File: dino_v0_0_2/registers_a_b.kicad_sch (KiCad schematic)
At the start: 11 parts, among them U31 74LS373, U32 74LS373, U33 74LS373, U35 74LS373, U41 74LS245, U42 74LS245, U43 74LS245, U44 74LS245, U5 74LS08, U57 74LS02, U66 74LS02

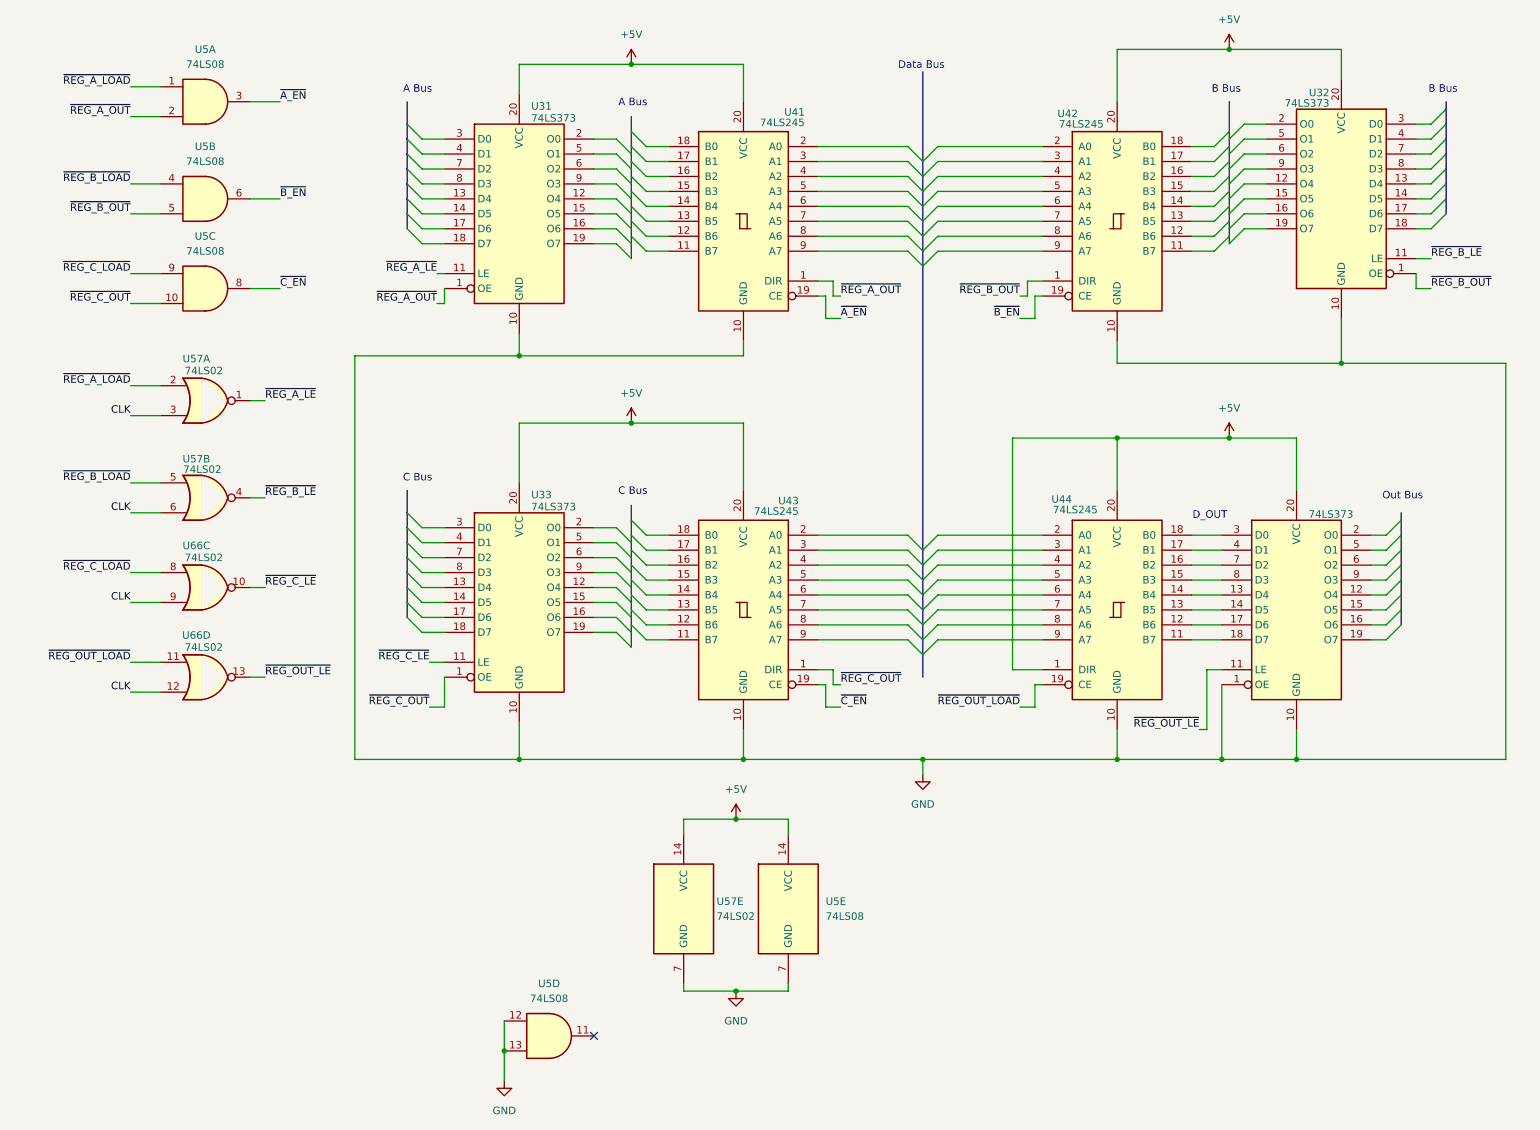
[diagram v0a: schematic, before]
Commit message: DINO v0.0.3: complete ALU/control-word, add MAR+reset sheets, wire reset circuit
ALU sheet: flags register moved from '173 (not in stock) to '273 + a '157
mux to emulate the missing load-enable pins; Z-detect built from a NOR+AND
De Morgan tree instead of a '260; ALU_CIN built from NAND(SA1,SA0) reusing
two already-placed spare gates instead of a dedicated XOR/'86. Sheet is
now fully wired and netlist-clean.

Control word sheet: all 16 CW bits assigned and wired (3x '138 decoders
for the load/source/misc fields, direct bus taps for HALT/PC_MAR_MUX/
PC_UP/END and the ALU SA[2:0] select). Found and fixed several cross-
sheet signal-name mismatches this uncovered (OUT_REG_LOAD/REG_OUT_LOAD,
PC_MAR_MUX/PC_MUX, T-state counter labels, a mirror-reversed IRB->ROM-
address buffer in microcode).

New: MAR and reset sheets, wired into the root hierarchy. Reset circuit
is a from-scratch design: RC+button+74HC14 Schmitt front end feeds the
async PRESET of the clock cluster's spare '74 half (U27B), synchronizing
release to CLK; its Q/~Q fan out to the flags register, the T-state
counter's clear, and (OR'd with the existing microcode-driven PC_CLEAR,
reusing spare gates on the same '02) the PC counters' clear.

Deprecated 7 schematic files no longer referenced by the root sheet's
hierarchy into dino_v0_0_2/deprecated/. Added docs/notes/kicad_netlist.py,
a .kicad_sch connectivity auditor (pin/net resolution incl. buses and
same-name local-label merging) used throughout this session to find the
above bugs; archived completed-work docs into docs/notes/Done/ and
rewrote dino_session_state.md as the current authoritative state+TODO.

Co-Authored-By: Claude Sonnet 5 <noreply@anthropic.com>
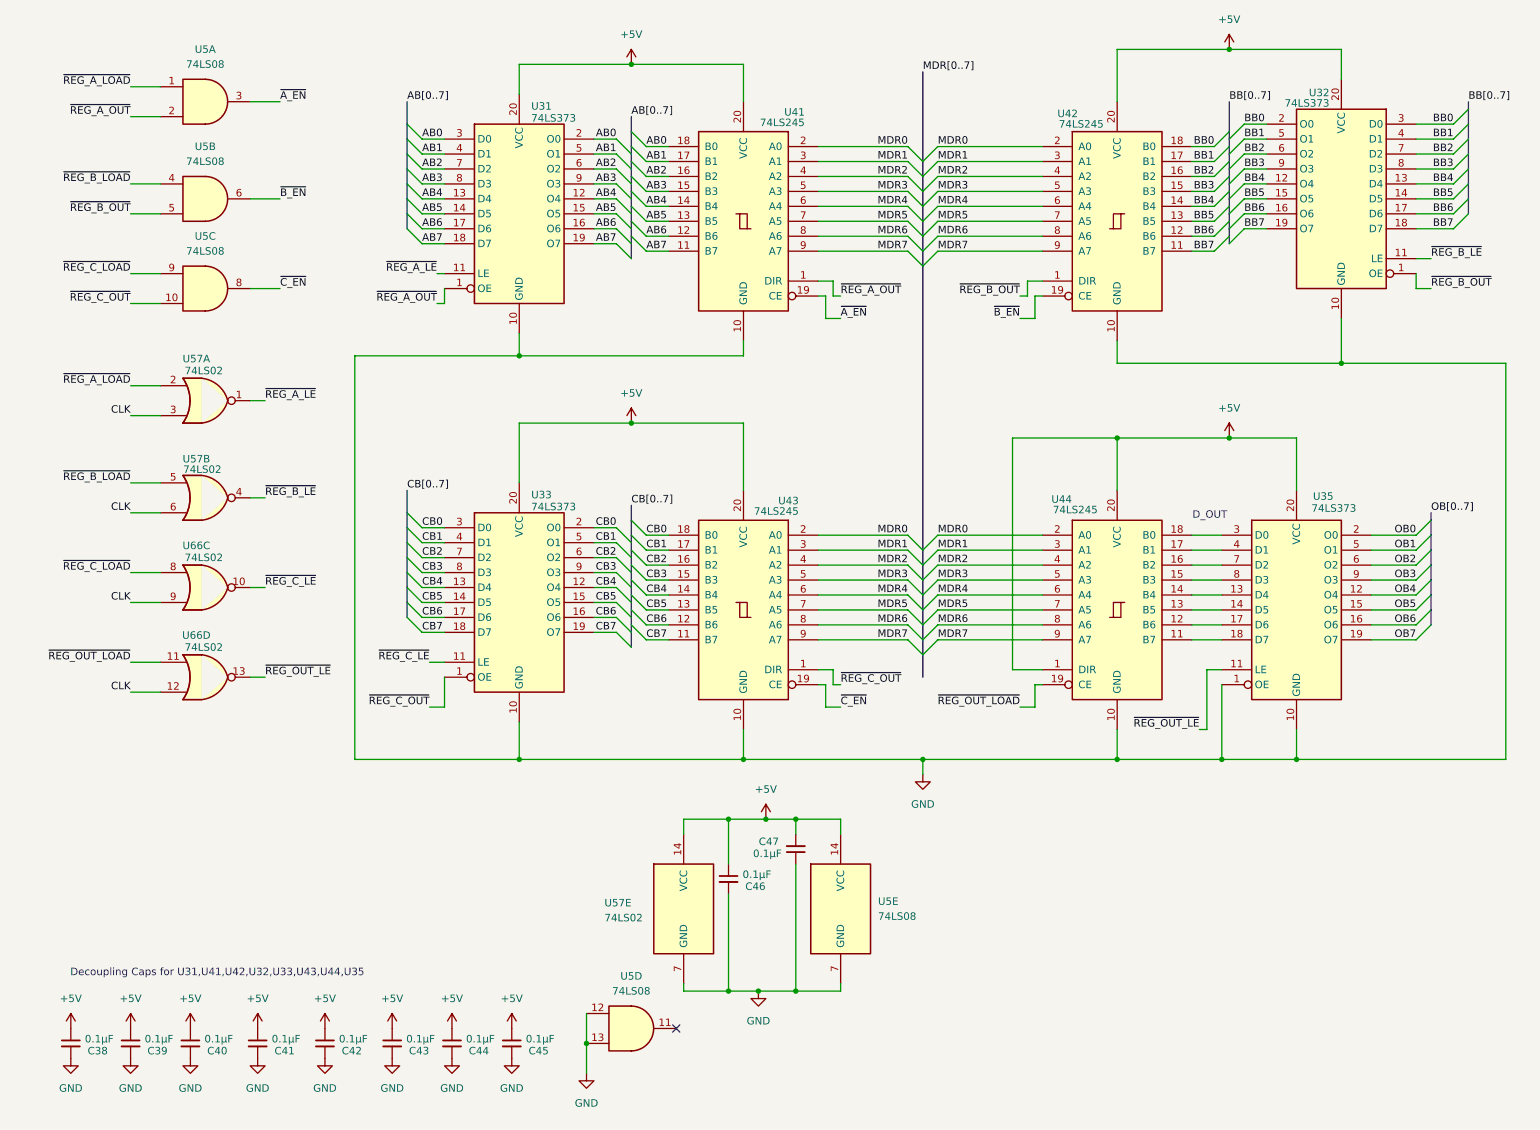
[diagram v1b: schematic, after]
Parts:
- added C38, C39, C40, C41, C42, C43, C44, C45, C46, C47: 0.1µF, symbol Device:C_Small
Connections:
- net +5V: now also C38.1, C39.1, C40.1, C41.1, C42.1, C43.1, C44.1, C45.1, C46.1, C47.2
- net GND: now also C38.2, C39.2, C40.2, C41.2, C42.2, C43.2, C44.2, C45.2, C46.2, C47.1
- net AB7: now reaches U41.11 (B7)
- net AB7: now also U31.18 (D7), U31.19 (O7)
- net AB6: now reaches U41.12 (B6)
- net AB6: now also U31.16 (O6), U31.17 (D6)
- net AB5: now reaches U41.13 (B5)
- net AB5: now also U31.14 (D5), U31.15 (O5)
- net AB4: now reaches U41.14 (B4)
- net AB4: now also U31.12 (O4), U31.13 (D4)
- net AB3: now reaches U41.15 (B3)
- net AB3: now also U31.8 (D3), U31.9 (O3)
- net AB2: now reaches U41.16 (B2)
- net AB2: now also U31.6 (O2), U31.7 (D2)
- net AB1: now reaches U41.17 (B1)
- net AB1: now also U31.4 (D1), U31.5 (O1)
- net AB0: now reaches U41.18 (B0)
- net AB0: now also U31.2 (O0), U31.3 (D0)
- net MDR0: now reaches U41.2 (A0)
- net MDR0: now also U42.2 (A0), U43.2 (A0), U44.2 (A0)
- net MDR1: now reaches U41.3 (A1)
- net MDR1: now also U42.3 (A1), U43.3 (A1), U44.3 (A1)
- net MDR2: now reaches U41.4 (A2)
- net MDR2: now also U42.4 (A2), U43.4 (A2), U44.4 (A2)
- net MDR3: now reaches U41.5 (A3)
- net MDR3: now also U42.5 (A3), U43.5 (A3), U44.5 (A3)
- net MDR4: now reaches U41.6 (A4)
- net MDR4: now also U42.6 (A4), U43.6 (A4), U44.6 (A4)
- net MDR5: now reaches U41.7 (A5)
- net MDR5: now also U42.7 (A5), U43.7 (A5), U44.7 (A5)
- net MDR6: now reaches U41.8 (A6)
- net MDR6: now also U42.8 (A6), U43.8 (A6), U44.8 (A6)
- net MDR7: now reaches U41.9 (A7)
- net MDR7: now also U42.9 (A7), U43.9 (A7), U44.9 (A7)
- net BB4: now reaches U32.12 (O4)
- net BB4: now also U32.13 (D4), U42.14 (B4)
- net BB5: now reaches U32.14 (D5)
- net BB5: now also U32.15 (O5), U42.13 (B5)
- net BB6: now reaches U32.16 (O6)
- net BB6: now also U32.17 (D6), U42.12 (B6)
- net BB7: now reaches U32.18 (D7)
- net BB7: now also U32.19 (O7), U42.11 (B7)
- net BB0: now reaches U32.2 (O0)
- net BB0: now also U32.3 (D0), U42.18 (B0)
- net BB1: now reaches U32.4 (D1)
- net BB1: now also U32.5 (O1), U42.17 (B1)
- net BB2: now reaches U32.6 (O2)
- net BB2: now also U32.7 (D2), U42.16 (B2)
- net BB3: now reaches U32.8 (D3)
- net BB3: now also U32.9 (O3), U42.15 (B3)
- net CB4: now reaches U33.12 (O4)
- net CB4: now also U33.13 (D4), U43.14 (B4)
- net CB5: now reaches U33.14 (D5)
- net CB5: now also U33.15 (O5), U43.13 (B5)
- net CB6: now reaches U33.16 (O6)
- net CB6: now also U33.17 (D6), U43.12 (B6)
- net CB7: now reaches U33.18 (D7)
- net CB7: now also U33.19 (O7), U43.11 (B7)
- net CB0: now reaches U33.2 (O0)
- net CB0: now also U33.3 (D0), U43.18 (B0)
- net CB1: now reaches U33.4 (D1)
- net CB1: now also U33.5 (O1), U43.17 (B1)
- net CB2: now reaches U33.6 (O2)
- net CB2: now also U33.7 (D2), U43.16 (B2)
- net CB3: now reaches U33.8 (D3)
- net CB3: now also U33.9 (O3), U43.15 (B3)
- net OB4: now reaches U35.12 (O4)
- net OB5: now reaches U35.15 (O5)
- net OB6: now reaches U35.16 (O6)
- net OB7: now reaches U35.19 (O7)
- net OB0: now reaches U35.2 (O0)
- net OB1: now reaches U35.5 (O1)
- net OB2: now reaches U35.6 (O2)
- net OB3: now reaches U35.9 (O3)
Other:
- note added: "Decoupling Caps for U31,U41,U42,U32,U33,U43,U44,U35"
- note removed: "A Bus"
- note removed: "B Bus"
- note removed: "C Bus"
- note removed: "Data Bus"
- note removed: "Out Bus"
- moved on the sheet: U5D, U5E
